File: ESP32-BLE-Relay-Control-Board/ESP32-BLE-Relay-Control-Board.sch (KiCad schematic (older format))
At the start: 6 parts, among them U1 ESP32-WROOM-32

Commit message: BLE RELAY UPDATE
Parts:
- added C1, C2, C3: C_Small, Capacitor_SMD:C_0805_2012Metric_Pad1.15x1.40mm_HandSolder, symbol Device:C_Small
- added D2: LED, LED_SMD:LED_0805_2012Metric, symbol Device:LED
- added R2: R_Small, Resistor_SMD:R_0603_1608Metric_Pad1.05x0.95mm_HandSolder, symbol Device:R_Small
- added SW1, SW2: SW_Push, Button_Switch_SMD:SW_DIP_SPSTx01_Slide_6.7x4.1mm_W6.73mm_P2.54mm_LowProfile_JPin, symbol Switch:SW_Push
- R1: renamed from R?; footprint (none) -> Resistor_SMD:R_0603_1608Metric_Pad1.05x0.95mm_HandSolder
- gave numbers to parts that had none: 4
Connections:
- net labels added: +3V3, +5V, EN, IN1, IO0, RX0, TX0, VCCQ
- net labels removed: in
- wire segments 16 -> 45
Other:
- moved on the sheet: K1, Q1, R1, U2

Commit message: relay added
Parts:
- removed D1: 1N4148WS, Diode_SMD:D_SOD-323, symbol Diode:1N4148WS
- added D1, D3: 1N4148W, Diode_SMD:D_SOD-123, symbol Diode:1N4148W
- added D4: LED, LED_SMD:LED_0805_2012Metric, symbol Device:LED
- added J1, J2: Conn_01x03, TerminalBlock:TerminalBlock_bornier-3_P5.08mm, symbol Connector_Generic:Conn_01x03
- added K2: SANYOU_SRD_Form_C, Relay_THT:Relay_SPDT_SANYOU_SRD_Series_Form_C, symbol Relay:SANYOU_SRD_Form_C
- added Q2: BC817, Package_TO_SOT_SMD:SOT-23, symbol Transistor_BJT:BC817
- added R3: R_Small, Resistor_SMD:R_0603_1608Metric_Pad1.05x0.95mm_HandSolder, symbol Device:R_Small
- added U3: EL817, Package_DIP:DIP-4_W7.62mm, symbol Isolator:EL817
- added U4: easyPower-5V, electroShri:easyPower-5V, symbol electroShri:easyPower-5V
- SW1, SW2: footprint Button_Switch_SMD:SW_DIP_SPSTx01_Slide_6.7x4.1mm_W6.73mm_P2.54mm_LowProfile_JPin -> Button_Switch_THT:SW_PUSH_6mm
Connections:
- net labels added: COM_1, COM_2, IN2
- wire segments 45 -> 72
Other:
- moved on the sheet: D2, K1, Q1, R1, U2

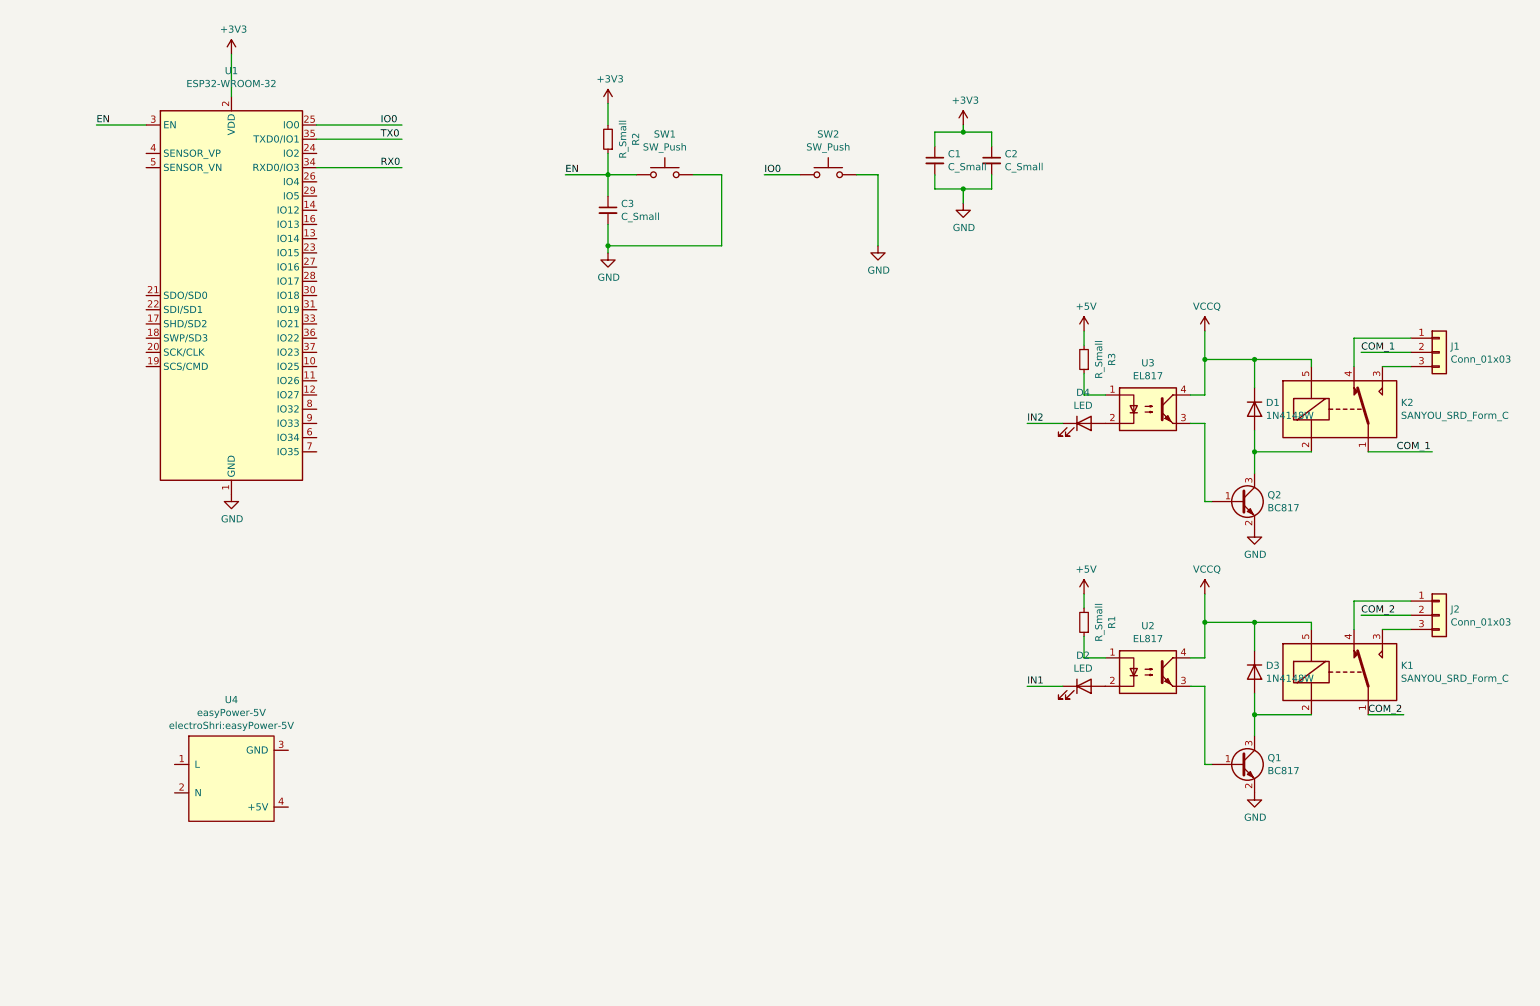
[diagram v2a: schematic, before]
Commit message: Power in connector added
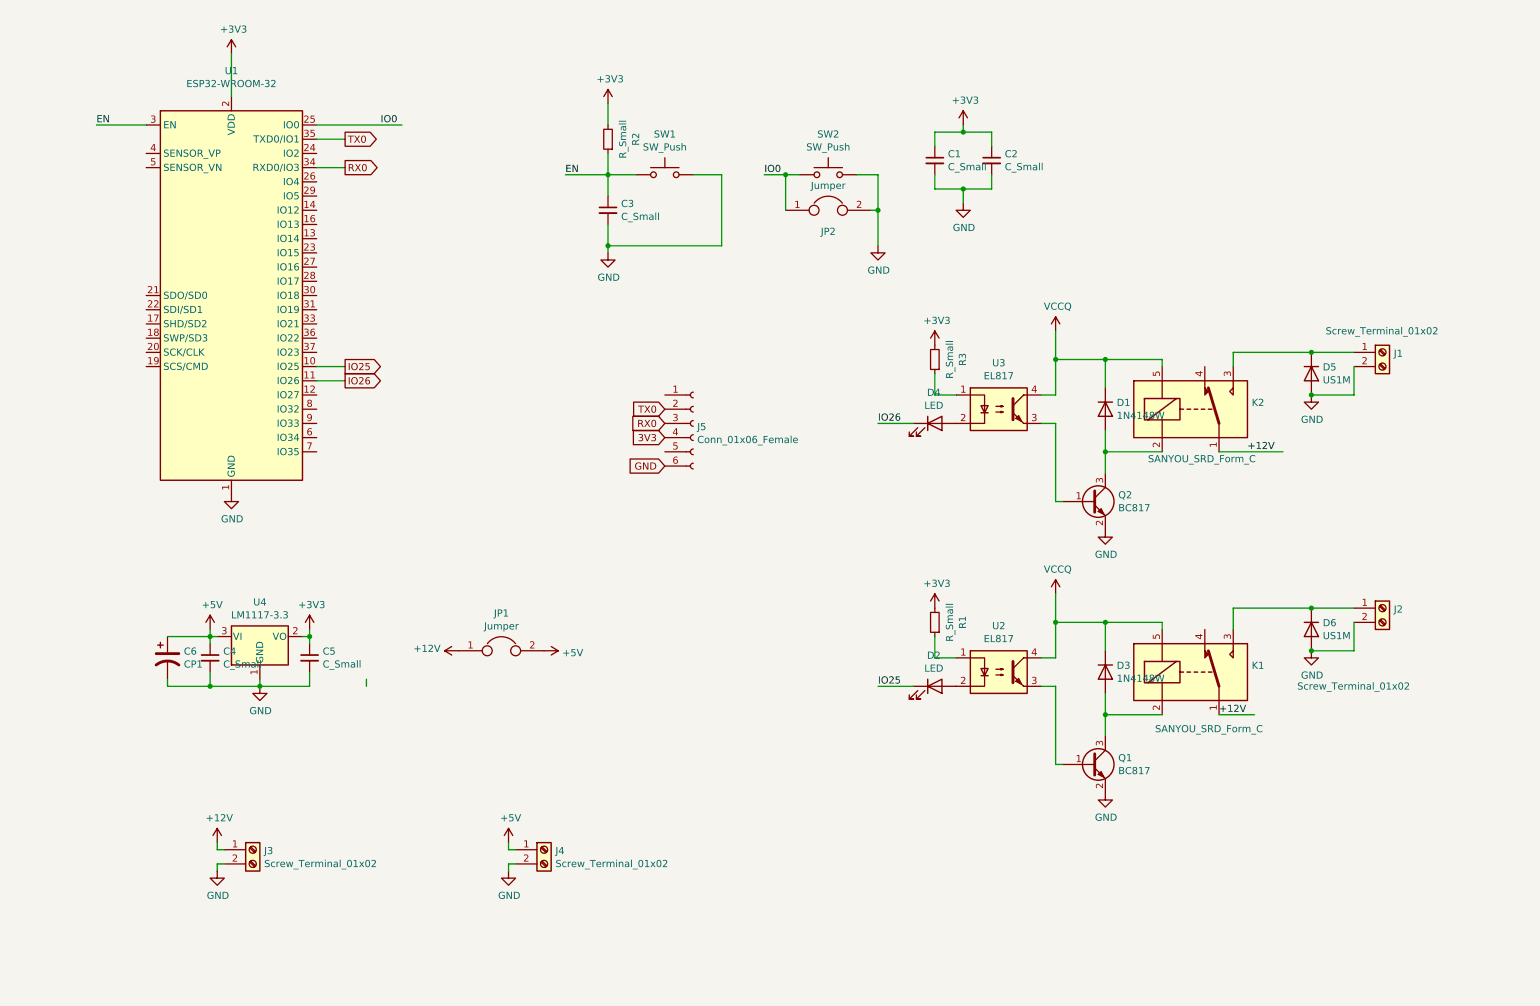
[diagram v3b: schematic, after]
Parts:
- removed J1, J2: Conn_01x03, TerminalBlock:TerminalBlock_bornier-3_P5.08mm, symbol Connector_Generic:Conn_01x03
- removed U4: easyPower-5V, electroShri:easyPower-5V, symbol electroShri:easyPower-5V
- added C4, C5: C_Small, Capacitor_SMD:C_0805_2012Metric_Pad1.15x1.40mm_HandSolder, symbol Device:C_Small
- added C6: CP1, Capacitor_THT:CP_Radial_D12.5mm_P7.50mm, symbol Device:CP1
- added D5, D6: US1M, Diode_SMD:D_SMA, symbol Diode:US1M
- added J1, J2, J3, J4: Screw_Terminal_01x02, TerminalBlock:TerminalBlock_bornier-2_P5.08mm, symbol Connector:Screw_Terminal_01x02
- added J5: Conn_01x06_Female, Connector_PinHeader_2.54mm:PinHeader_1x06_P2.54mm_Vertical, symbol Connector:Conn_01x06_Female
- added JP1, JP2: Jumper, TestPoint:TestPoint_2Pads_Pitch2.54mm_Drill0.8mm, symbol Device:Jumper
- added U4: LM1117-3.3, Package_TO_SOT_SMD:SOT-223-3_TabPin2, symbol Regulator_Linear:LM1117-3.3
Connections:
- net labels added: +12V, 3V3, IO25, IO26
- net labels removed: COM_1, COM_2, IN1, IN2
- wire segments 72 -> 101
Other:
- moved on the sheet: D1, D2, D3, D4, K1, K2, Q1, Q2, R1, R3, U2, U3

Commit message: 5V LDO Added
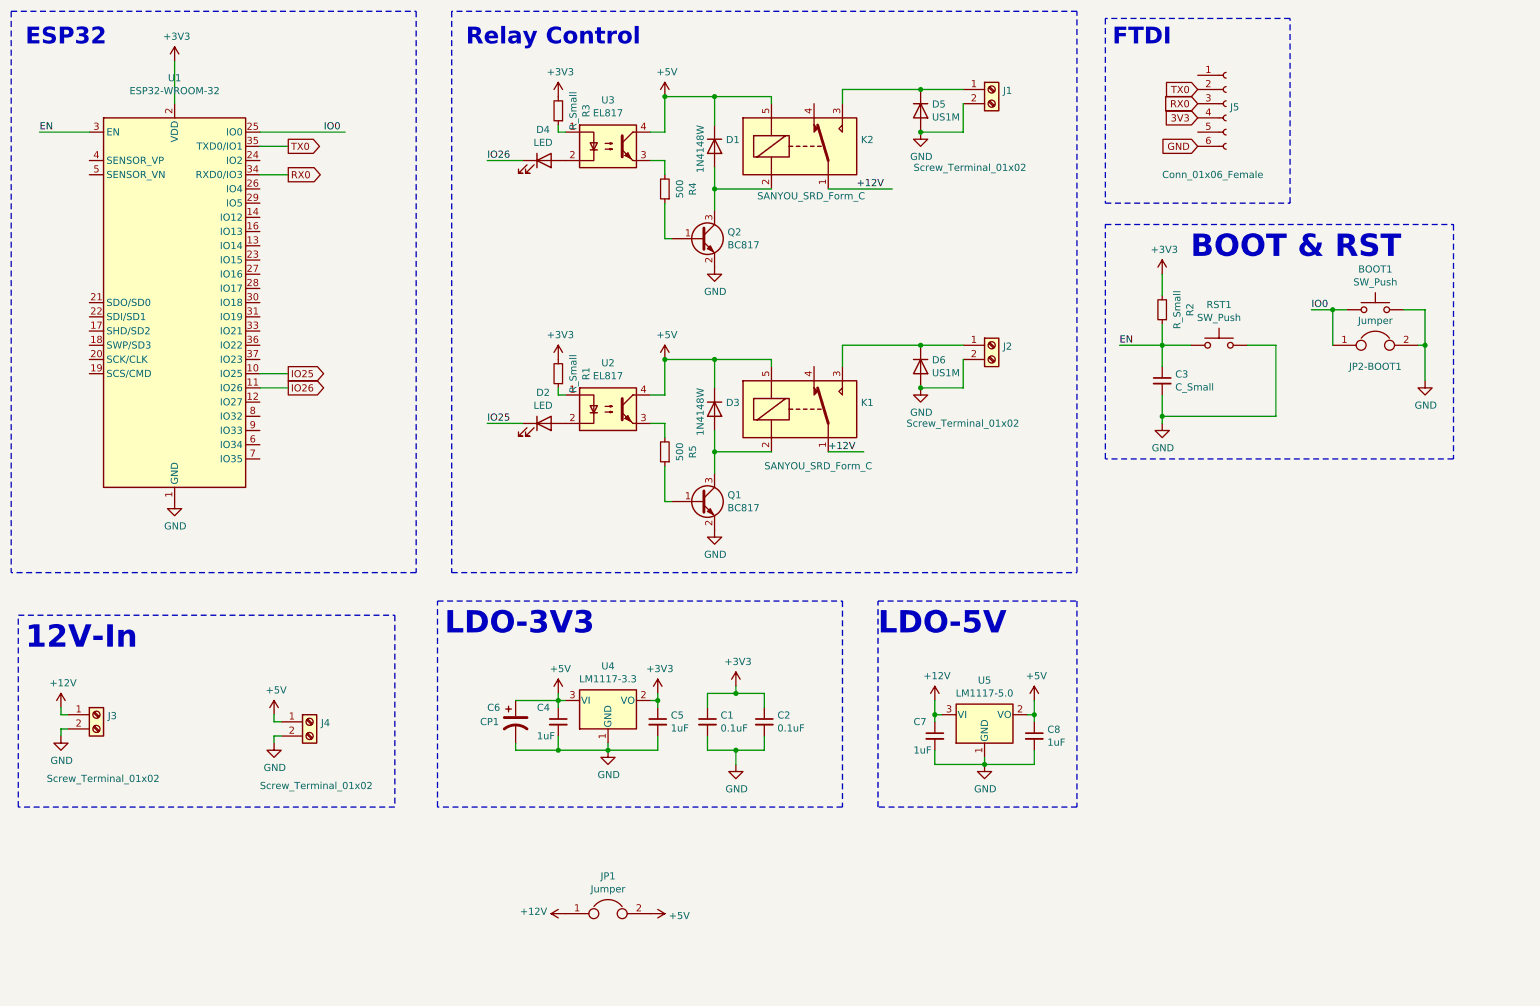
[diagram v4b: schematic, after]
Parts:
- added C7, C8: 1uF, Capacitor_SMD:C_0805_2012Metric_Pad1.15x1.40mm_HandSolder, symbol Device:C_Small
- added R4, R5: 500, Resistor_SMD:R_0603_1608Metric_Pad1.05x0.95mm_HandSolder, symbol Device:R_Small
- added U5: LM1117-5.0, Package_TO_SOT_SMD:SOT-223-3_TabPin2, symbol Regulator_Linear:LM1117-5.0
- C1, C2: value C_Small -> 0.1uF
- C4, C5: value C_Small -> 1uF
- renumbered SW2 to BOOT1, JP2 to JP2-BOOT1, SW1 to RST1
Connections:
- net labels removed: VCCQ
- wire segments 101 -> 111
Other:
- note added: "12V-In"
- note added: "BOOT & RST"
- note added: "ESP32"
- note added: "FTDI"
- note added: "LDO-3V3"
- note added: "LDO-5V"
- note added: "Relay Control"
- moved on the sheet: BOOT1, C1, C2, C3, C4, C5, C6, D1, D2, D3, D4, D5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

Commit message: UPDATE, logos added to board
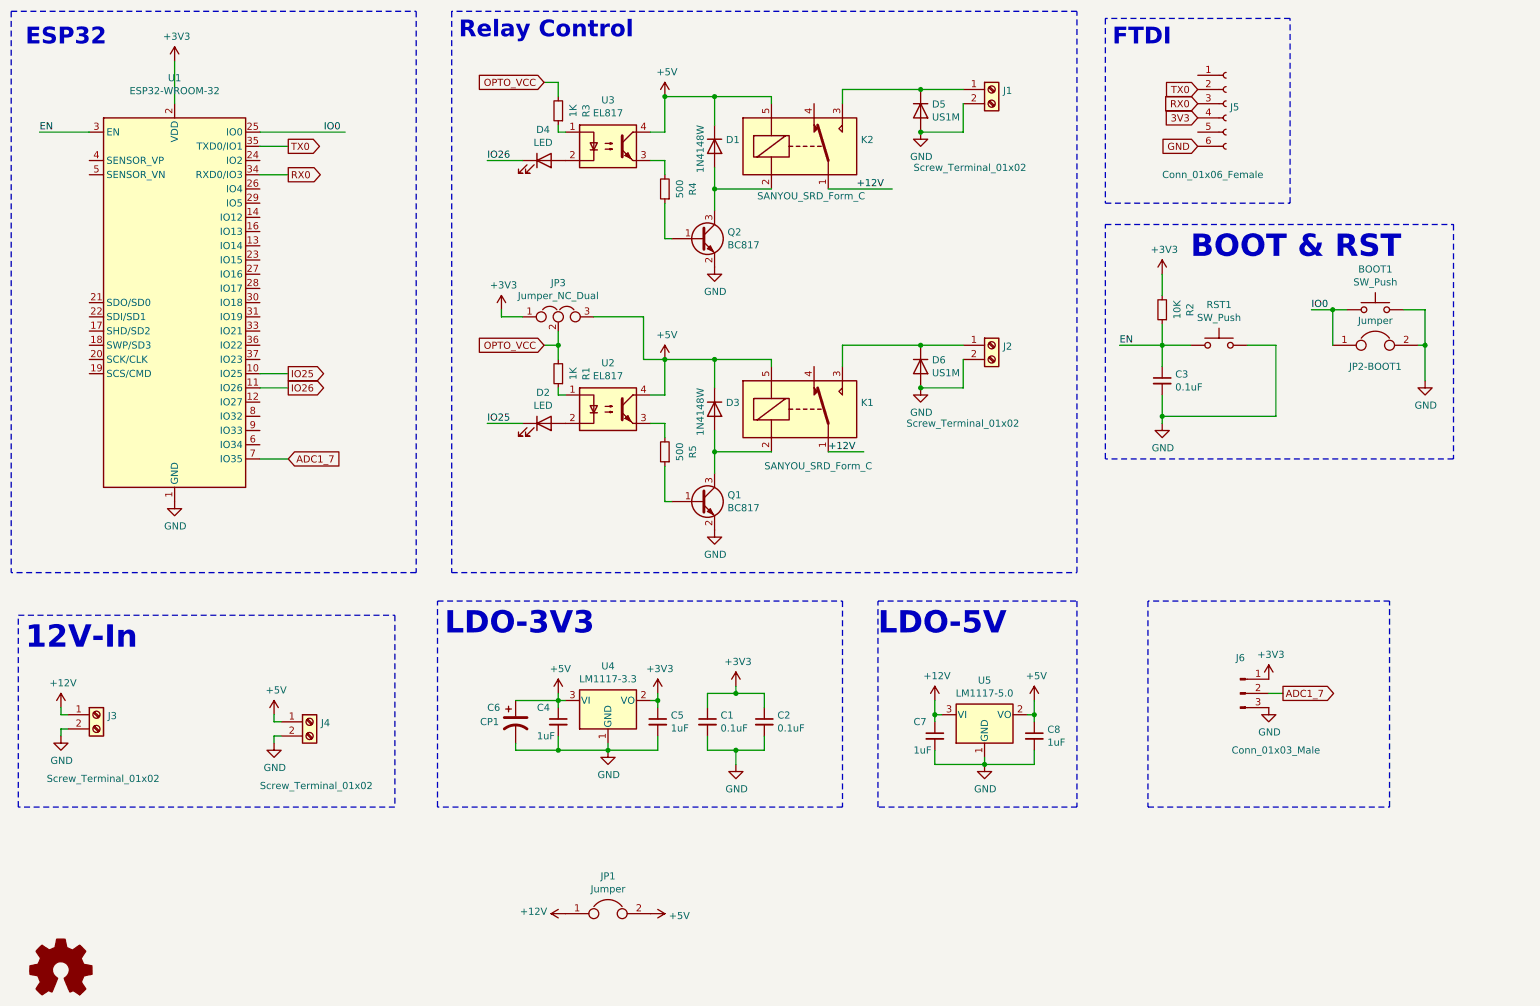
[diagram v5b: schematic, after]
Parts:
- added J6: Conn_01x03_Male, Connector_PinSocket_2.54mm:PinSocket_1x03_P2.54mm_Vertical, symbol Connector:Conn_01x03_Male
- added JP3: Jumper_NC_Dual, Jumper:SolderJumper-3_P1.3mm_Bridged12_RoundedPad1.0x1.5mm_NumberLabels, symbol Device:Jumper_NC_Dual
- C3: value C_Small -> 0.1uF
- R1, R3: value R_Small -> 1K
- R2: value R_Small -> 10K
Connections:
- net +3V3: now also J6.1 (Pin_1), JP3.1; no longer R1.2, R3.2
- net +5V: now also JP3.3
- net GND: now also J6.3 (Pin_3)
- net ADC1_7: now reaches U1.7 (IO35)
- net ADC1_7: now also J6.2 (Pin_2)
- new net OPTO_VCC: JP3.2, R1.2, R3.2
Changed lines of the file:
@@
 P 4600 3200
 F 0 "R1" V 4404 3200 50  0000 C CNN
-F 1 "R_Small" V 4495 3200 50  0000 C CNN
+F 1 "1K" V 4495 3200 50  0000 C CNN
 F 2 "Resistor_SMD:R_0603_1608Metric_Pad1.05x0.95mm_HandSolder" H 4600 3200 50  0001 C CNN
 F 3 "~" H 4600 3200 50  0001 C CNN
@@
 P 8850 2750
 F 0 "R2" V 8654 2750 50  0000 C CNN
-F 1 "R_Small" V 8745 2750 50  0000 C CNN
+F 1 "10K" V 8745 2750 50  0000 C CNN
 F 2 "Resistor_SMD:R_0603_1608Metric_Pad1.05x0.95mm_HandSolder" H 8850 2750 50  0001 C CNN
 F 3 "~" H 8850 2750 50  0001 C CNN
@@
 P 8850 3250
 F 0 "C3" H 8942 3296 50  0000 L CNN
-F 1 "C_Small" H 8942 3205 50  0000 L CNN
+F 1 "0.1uF" H 8942 3205 50  0000 L CNN
 F 2 "Capacitor_SMD:C_0805_2012Metric_Pad1.15x1.40mm_HandSolder" H 8850 3250 50  0001 C CNN
 F 3 "~" H 8850 3250 50  0001 C CNN
@@
 P 4600 1350
 F 0 "R3" V 4404 1350 50  0000 C CNN
-F 1 "R_Small" V 4495 1350 50  0000 C CNN
+F 1 "1K" V 4495 1350 50  0000 C CNN
 F 2 "Resistor_SMD:R_0603_1608Metric_Pad1.05x0.95mm_HandSolder" H 4600 1350 50  0001 C CNN
 F 3 "~" H 4600 1350 50  0001 C CNN
@@
 GND
 $Comp
-L power:+3V3 #PWR0112
-U 1 1 5F38901D
-P 4600 3100
-F 0 "#PWR0112" H 4600 2950 50  0001 C CNN
-F 1 "+3V3" H 4615 3273 50  0000 C CNN
-F 2 "" H 4600 3100 50  0001 C CNN
-F 3 "" H 4600 3100 50  0001 C CNN
-	1    4600 3100
-	1    0    0    -1
-$EndComp
-$Comp
-L power:+3V3 #PWR0113
-U 1 1 5F38CC4E
-P 4600 1250
-F 0 "#PWR0113" H 4600 1100 50  0001 C CNN
-F 1 "+3V3" H 4615 1423 50  0000 C CNN
-F 2 "" H 4600 1250 50  0001 C CNN
-F 3 "" H 4600 1250 50  0001 C CNN
-	1    4600 1250
-	1    0    0    -1
-$EndComp
-$Comp
 L Device:C_Small C7
 U 1 1 5F2E2D0E
@@
 Text Notes 850  900  0    118  ~ 24
 ESP32
-Text Notes 3950 900  0    118  ~ 24
+Text Notes 3900 850  0    118  ~ 24
 Relay Control
 Text Notes 8500 900  0    118  ~ 24
@@
 Text Notes 850  5150 0    157  ~ 31
 12V-In
+Text GLabel 4500 3000 0    50   Input ~ 0
+OPTO_VCC
+Wire Wire Line
+	4600 1150 4600 1250
+Text GLabel 4500 1150 0    50   Input ~ 0
+OPTO_VCC
+Wire Wire Line
+	4500 1150 4600 1150
+Wire Wire Line
+	4500 3000 4600 3000
+Wire Wire Line
+	4600 3000 4600 3100
+$Comp
+L Device:Jumper_NC_Dual JP3
+U 1 1 5F2D26F2
+P 4600 2800
+F 0 "JP3" H 4600 3039 50  0000 C CNN
+F 1 "Jumper_NC_Dual" H 4600 2948 50  0000 C CNN
+F 2 "Jumper:SolderJumper-3_P1.3mm_Bridged12_RoundedPad1.0x1.5mm_NumberLabels" H 4600 2800 50  0001 C CNN
+F 3 "~" H 4600 2800 50  0001 C CNN
+	1    4600 2800
+	1    0    0    -1
+$EndComp
+Wire Wire Line
+	4600 2900 4600 3000
+Connection ~ 4600 3000
+Wire Wire Line
+	4850 2800 5200 2800
+Wire Wire Line
+	5200 2800 5200 3100
+Wire Wire Line
+	5200 3100 5350 3100
+$Comp
+L power:+3V3 #PWR0112
+U 1 1 5F2DC372
+P 4200 2750
+F 0 "#PWR0112" H 4200 2600 50  0001 C CNN
+F 1 "+3V3" H 4215 2923 50  0000 C CNN
+F 2 "" H 4200 2750 50  0001 C CNN
+F 3 "" H 4200 2750 50  0001 C CNN
+	1    4200 2750
+	1    0    0    -1
+$EndComp
+Wire Wire Line
+	4200 2750 4200 2800
+Wire Wire Line
+	4200 2800 4350 2800
+Wire Wire Line
+	2500 3800 2700 3800
+Text GLabel 2700 3800 2    50   Input ~ 0
+ADC1_7
+$Comp
+L Connector:Conn_01x03_Male J6
+U 1 1 5F35C13D
+P 9400 5450
+F 0 "J6" H 9400 5700 50  0000 C CNN
+F 1 "Conn_01x03_Male" H 9650 5050 50  0000 C CNN
+F 2 "Connector_PinSocket_2.54mm:PinSocket_1x03_P2.54mm_Vertical" H 9400 5450 50  0001 C CNN
+F 3 "~" H 9400 5450 50  0001 C CNN
+	1    9400 5450
+	1    0    0    -1
+$EndComp
+Wire Wire Line
+	9600 5450 9700 5450
+Text GLabel 9700 5450 2    50   Output ~ 0
+ADC1_7
+$Comp
+L power:GND #PWR02
+U 1 1 5F361F71
+P 9600 5550
+F 0 "#PWR02" H 9600 5300 50  0001 C CNN
+F 1 "GND" H 9605 5377 50  0000 C CNN
+F 2 "" H 9600 5550 50  0001 C CNN
+F 3 "" H 9600 5550 50  0001 C CNN
+	1    9600 5550
+	1    0    0    -1
+$EndComp
+$Comp
+L power:+3V3 #PWR01
+U 1 1 5F36230E
+P 9600 5350
+F 0 "#PWR01" H 9600 5200 50  0001 C CNN
+F 1 "+3V3" H 9615 5523 50  0000 C CNN
+F 2 "" H 9600 5350 50  0001 C CNN
+F 3 "" H 9600 5350 50  0001 C CNN
+	1    9600 5350
+	1    0    0    -1
+$EndComp
+Wire Notes Line
+	8750 4800 8750 6250
+Wire Notes Line
+	8750 6250 10450 6250
+Wire Notes Line
+	10450 6250 10450 4800
+Wire Notes Line
+	10450 4800 8750 4800
+$Comp
+L Graphic:Logo_Open_Hardware_Small #LOGO1
+U 1 1 5F3779F4
+P 1100 7400
+F 0 "#LOGO1" H 1100 7675 50  0001 C CNN
+F 1 "Logo_Open_Hardware_Small" H 1100 7175 50  0001 C CNN
+F 2 "" H 1100 7400 50  0001 C CNN
+F 3 "~" H 1100 7400 50  0001 C CNN
+	1    1100 7400
+	1    0    0    -1
+$EndComp
 $EndSCHEMATC
